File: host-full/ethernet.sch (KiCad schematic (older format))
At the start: 140 parts, among them J1 CONN_INTEGRALSTICK_MCU_HOST, J2 CONN_INTEGRALSTICK_FPGA_HOST, J3 0826-1G1T-23-F, J4 0826-1G1T-23-F, J5 0826-1G1T-23-F, J6 0826-1G1T-23-F, U1 KSZ9031RNX, U2 KSZ9031RNX, U3 ECS-1612MV-250-CN-TR, U4 ECS-1612MV-250-CN-TR, U5 KSZ9031RNX, U6 ECS-1612MV-250-CN-TR

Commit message: Finished initial schematic review
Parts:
- added C76, C79, C82: 4.7 uF, symbol device:C
- added C77, C78, C80, C81, C83, C84: 0.47 uF, symbol device:C
- added L10, L8, L9: 600R @ 100 MHz, symbol passive-azonenberg:INDUCTOR_PWROUT
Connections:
- net 1V2: now also L10.2, L8.2, L9.2
- net 1V8: no longer R24.1, R36.1
- net 3V3: now also R24.1, R36.1
- net ETH1_A1V2: now also C79.1, C80.1, C81.1, L9.1
- net ETH1_LED1_N_1V8: now also J2.43 (IO_1V8_CLK); no longer J2.67 (IO_1V8)
- net ETH1_LED2_N_1V8: now also J2.67 (IO_1V8); no longer J2.68 (IO_1V8)
- net ETH1_MDC: now also J2.56 (IO_1V8); no longer J2.53 (IO_1V8)
- net ETH1_MDIO: now also J2.59 (IO_1V8); no longer J2.50 (IO_1V8)
- net ETH1_RST_N: now also J2.53 (IO_1V8); no longer J2.56 (IO_1V8)
- net ETH1_RXD0: now also J2.65 (IO_1V8); no longer J2.44 (IO_1V8)
- net ETH1_RXD1: now also J2.62 (IO_1V8); no longer J2.47 (IO_1V8)
- net ETH1_RXD2: now also J2.61 (IO_1V8); no longer J2.48 (IO_1V8)
- net ETH1_RXD3: now also J2.60 (IO_1V8); no longer J2.49 (IO_1V8)
- net ETH1_RX_CLK: now also J2.41 (IO_1V8_CLK); no longer J2.43 (IO_1V8_CLK)
- net ETH1_RX_DV: now also J2.66 (IO_1V8); no longer J2.42 (IO_1V8)
- net ETH1_TXD0: now also J2.42 (IO_1V8); no longer J2.66 (IO_1V8)
- net ETH1_TXD1: now also J2.44 (IO_1V8); no longer J2.65 (IO_1V8)
- net ETH1_TXD2: now also J2.47 (IO_1V8); no longer J2.62 (IO_1V8)
- net ETH1_TXD3: now also J2.48 (IO_1V8); no longer J2.61 (IO_1V8)
- net ETH1_TX_CLK: now also J2.49 (IO_1V8); no longer J2.60 (IO_1V8)
- net ETH1_TX_EN: now also J2.50 (IO_1V8); no longer J2.59 (IO_1V8)
- net ETH2_A1V2: now also C76.1, C77.1, C78.1, L8.1
- net ETH3_A1V2: now also C82.1, C83.1, C84.1, L10.1
- net GND: now also C76.2, C77.2, C78.2, C79.2, C80.2, C81.2, C82.2, C83.2, C84.2
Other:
- moved on the sheet: C3, C39, C7

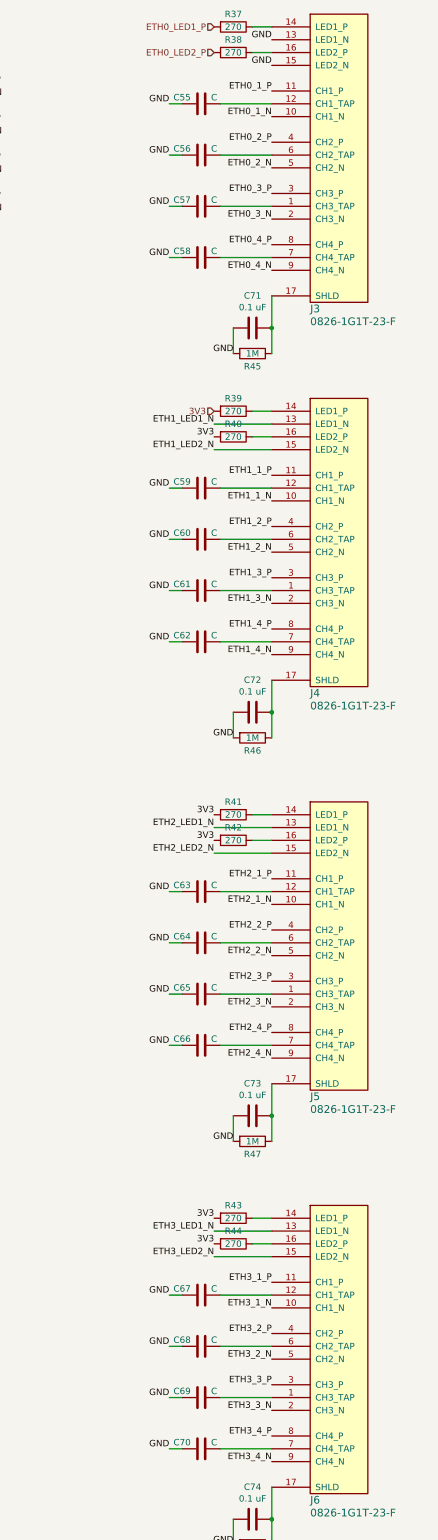
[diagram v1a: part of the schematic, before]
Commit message: Initial layout on host-full. Rough floorplan is finalized, all MCU PMODs routed.
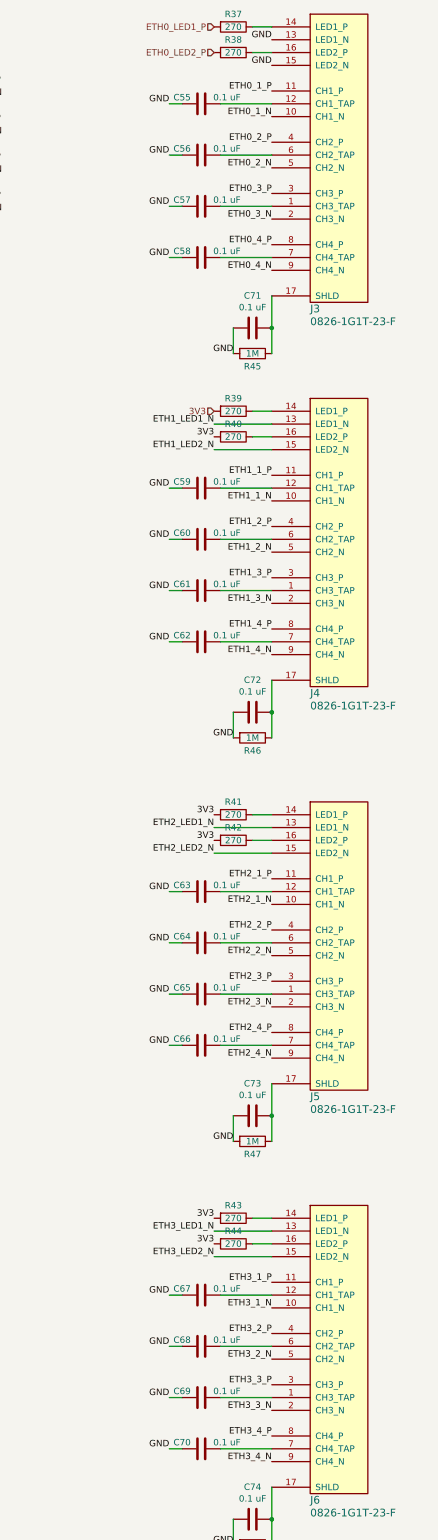
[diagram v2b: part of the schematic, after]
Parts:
- C1, C11, C13, C15, C2, C3, C37, C38, C39, C4, C40, C41, C43, C5, C6, C7, C76, C79, C8, C82, C9: footprint (none) -> azonenberg_pcb:EIA_0603_CAP_NOSILK
- C10, C12, C14, C16, C17, C18, C19, C20, C21, C22, C23, C24, C25, C26, C27, C28, C29, C30, C31, C32, C33, C34, C35, C36, C42, C44, C45, C46, C47, C48, C49, C50, C51, C52, C53, C54, C71, C72, C73, C74, C77, C78, C80, C81, C83, C84, L1, L10, L2, L3, L4, L5, L6, L8, L9: footprint (none) -> azonenberg_pcb:EIA_0402_CAP_NOSILK
- C55, C56, C57, C58, C59, C60, C61, C62, C63, C64, C65, C66, C67, C68, C69, C70: value C -> 0.1 uF; footprint (none) -> azonenberg_pcb:EIA_0402_CAP_NOSILK
- J1, J2: footprint (none) -> azonenberg_pcb:CONN_SAMTEC_QSH-060-01-L-D-A
- J3, J4, J5, J6: footprint (none) -> azonenberg_pcb:CONN_BELFUSE_0826_1G1T_23_F
- R1, R10, R11, R12, R13, R14, R15, R16, R17, R18, R19, R2, R20, R21, R22, R23, R24, R25, R26, R27, R28, R29, R3, R30, R31, R32, R33, R34, R35, R36, R37, R38, R39, R4, R40, R41, R42, R43, R44, R45, R46, R47, R48, R5, R6, R7, R8, R9: footprint (none) -> azonenberg_pcb:EIA_0402_RES_NOSILK
- U1, U2, U5: footprint (none) -> azonenberg_pcb:QFN_48_0.5MM_7x7MM
- U3, U4, U6: footprint (none) -> azonenberg_pcb:OSCILLATOR_1.6x1.2

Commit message: Continued host-full layout. Almost all PHY RGMII routing done
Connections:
- net 1V8: now also C38.1, C42.1, C46.1, C54.1, R36.1, U5.16 (DVDDH), U5.34 (DVDDH), U5.40 (DVDDH), U6.1 (E/D#), U6.4 (Vdd); no longer C10.1, C18.1, C2.1, C35.1, R17.1, R23.1, R8.1, U1.16 (DVDDH), U1.34 (DVDDH), U1.40 (DVDDH), U3.1 (E/D#), U3.4 (Vdd)
- net 3V3: now also C10.1, C18.1, C2.1, C35.1, R17.1, R23.1, R8.1, U1.16 (DVDDH), U1.34 (DVDDH), U1.40 (DVDDH), U3.1 (E/D#), U3.4 (Vdd); no longer C38.1, C42.1, C46.1, C54.1, R36.1, U5.16 (DVDDH), U5.34 (DVDDH), U5.40 (DVDDH), U6.1 (E/D#), U6.4 (Vdd)
- net ETH0_1_N: now also J1.4 (ETH_A_P); no longer J1.6 (ETH_A_N)
- net ETH0_1_P: now also J1.6 (ETH_A_N); no longer J1.4 (ETH_A_P)
- net ETH0_3_N: now also J1.16 (ETH_C_P); no longer J1.18 (ETH_C_N)
- net ETH0_3_P: now also J1.18 (ETH_C_N); no longer J1.16 (ETH_C_P)
- net ETH1_2_N: now also U1.5 (TXRXP_B); no longer U1.6 (TXRXM_B)
- net ETH1_2_P: now also U1.6 (TXRXM_B); no longer U1.5 (TXRXP_B)
- net ETH1_4_N: now also U1.10 (TXRXP_D); no longer U1.11 (TXRXM_D)
- net ETH1_4_P: now also U1.11 (TXRXM_D); no longer U1.10 (TXRXP_D)
- net ETH1_LED1_N: now also R19.2, U1.17 (LED1/PHYAD0); no longer J2.95 (IO_3V3)
- net ETH1_LED2_N: now also R1.2, U1.15 (LED2/PHYAD1); no longer J2.96 (IO_3V3)
- net ETH1_MDC: now also J2.79 (IO_3V3); no longer J2.56 (IO_1V8)
- net ETH1_MDIO: now also J2.77 (IO_3V3); no longer J2.59 (IO_1V8)
- net ETH1_RST_N: now also J2.73 (IO_3V3); no longer J2.53 (IO_1V8)
- net ETH1_RXD0: now also J2.85 (IO_3V3); no longer J2.65 (IO_1V8)
- net ETH1_RXD1: now also J2.89 (IO_3V3); no longer J2.62 (IO_1V8)
- net ETH1_RXD2: now also J2.91 (IO_3V3); no longer J2.61 (IO_1V8)
- net ETH1_RXD3: now also J2.95 (IO_3V3); no longer J2.60 (IO_1V8)
- net ETH1_RX_CLK: now also J2.71 (IO_3V3_CLK); no longer J2.41 (IO_1V8_CLK)
- net ETH1_RX_DV: now also J2.83 (IO_3V3); no longer J2.66 (IO_1V8)
- net ETH1_TXD0: now also J2.119 (IO_3V3); no longer J2.42 (IO_1V8)
- net ETH1_TXD1: now also J2.115 (IO_3V3); no longer J2.44 (IO_1V8)
- net ETH1_TXD2: now also J2.113 (IO_3V3); no longer J2.47 (IO_1V8)
- net ETH1_TXD3: now also J2.103 (IO_3V3); no longer J2.48 (IO_1V8)
- net ETH1_TX_CLK: now also J2.101 (IO_3V3); no longer J2.49 (IO_1V8)
- net ETH1_TX_EN: now also J2.97 (IO_3V3); no longer J2.50 (IO_1V8)
- net ETH2_2_N: now also U2.5 (TXRXP_B); no longer U2.6 (TXRXM_B)
- net ETH2_2_P: now also U2.6 (TXRXM_B); no longer U2.5 (TXRXP_B)
- net ETH2_4_N: now also U2.10 (TXRXP_D); no longer U2.11 (TXRXM_D)
- net ETH2_4_P: now also U2.11 (TXRXM_D); no longer U2.10 (TXRXP_D)
- net ETH2_MDC: now also J2.86 (IO_3V3); no longer J2.90 (IO_3V3)
- net ETH2_MDIO: now also J2.84 (IO_3V3); no longer J2.91 (IO_3V3)
- net ETH2_RST_N: now also J2.80 (IO_3V3); no longer J2.92 (IO_3V3)
- net ETH2_RXD0: now also J2.92 (IO_3V3); no longer J2.86 (IO_3V3)
- net ETH2_RXD1: now also J2.96 (IO_3V3); no longer J2.85 (IO_3V3)
- net ETH2_RXD2: now also J2.98 (IO_3V3); no longer J2.84 (IO_3V3)
- net ETH2_RXD3: now also J2.102 (IO_3V3); no longer J2.83 (IO_3V3)
- net ETH2_RX_CLK: now also J2.72 (IO_3V3_CLK); no longer J2.71 (IO_3V3_CLK)
- net ETH2_RX_DV: now also J2.90 (IO_3V3); no longer J2.89 (IO_3V3)
- net ETH2_TXD0: now also J2.120 (IO_3V3); no longer J2.73 (IO_3V3)
- net ETH2_TXD1: now also J2.116 (IO_3V3); no longer J2.74 (IO_3V3)
- net ETH2_TXD2: now also J2.114 (IO_3V3); no longer J2.77 (IO_3V3)
- net ETH2_TXD3: now also J2.110 (IO_3V3); no longer J2.78 (IO_3V3)
- net ETH2_TX_CLK: now also J2.108 (IO_3V3); no longer J2.79 (IO_3V3)
- net ETH2_TX_EN: now also J2.104 (IO_3V3); no longer J2.80 (IO_3V3)
- net ETH3_2_N: now also U5.5 (TXRXP_B); no longer U5.6 (TXRXM_B)
- net ETH3_2_P: now also U5.6 (TXRXM_B); no longer U5.5 (TXRXP_B)
- net ETH3_4_N: now also U5.10 (TXRXP_D); no longer U5.11 (TXRXM_D)
- net ETH3_4_P: now also U5.11 (TXRXM_D); no longer U5.10 (TXRXP_D)
- net ETH3_LED1_N: now also J2.78 (IO_3V3); no longer R34.2, U5.17 (LED1/PHYAD0)
- net ETH3_LED2_N: now also J2.74 (IO_3V3); no longer R25.2, U5.15 (LED2/PHYAD1)
- net ETH3_MDC: now also J2.43 (IO_1V8_CLK); no longer J2.116 (IO_3V3)
- net ETH3_MDIO: now also J2.42 (IO_1V8); no longer J2.119 (IO_3V3)
- net ETH3_RST_N: now also J2.44 (IO_1V8); no longer J2.120 (IO_3V3)
- net ETH3_RXD0: now also J2.49 (IO_1V8); no longer J2.114 (IO_3V3)
- net ETH3_RXD1: now also J2.53 (IO_1V8); no longer J2.113 (IO_3V3)
- net ETH3_RXD2: now also J2.55 (IO_1V8); no longer J2.110 (IO_3V3)
- net ETH3_RXD3: now also J2.59 (IO_1V8); no longer J2.108 (IO_3V3)
- net ETH3_RX_CLK: now also J2.41 (IO_1V8_CLK); no longer J2.72 (IO_3V3_CLK)
- net ETH3_RX_DV: now also J2.47 (IO_1V8); no longer J2.115 (IO_3V3)
- net ETH3_TXD0: now also J2.67 (IO_1V8); no longer J2.97 (IO_3V3)
- net ETH3_TXD1: now also J2.65 (IO_1V8); no longer J2.98 (IO_3V3)
- net ETH3_TXD2: now also J2.61 (IO_1V8); no longer J2.101 (IO_3V3)
- net ETH3_TXD3: now also J2.68 (IO_1V8); no longer J2.102 (IO_3V3)
- net ETH3_TX_CLK: now also J2.66 (IO_1V8); no longer J2.103 (IO_3V3)
- net ETH3_TX_EN: now also J2.62 (IO_1V8); no longer J2.104 (IO_3V3)
- net ETH3_LED1_N_1V8: now reaches J2.54 (IO_1V8)
- net ETH3_LED1_N_1V8: now also R34.2, U5.17 (LED1/PHYAD0)
- removed net ETH1_LED1_N_1V8: J2.43 (IO_1V8_CLK), R19.2, U1.17 (LED1/PHYAD0)
- removed net ETH1_LED2_N_1V8: J2.67 (IO_1V8), R1.2, U1.15 (LED2/PHYAD1)
- new net ETH3_LED2_N_1V8: J2.50 (IO_1V8), R25.2, U5.15 (LED2/PHYAD1)
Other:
- note added: "Pairs 1/3 swapped for routability"
- note added: "Pairs 2/4 swapped for routability"
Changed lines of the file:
@@
 Sheet 4 4
 Title "INTEGRALSTICK Full Host"
-Date "2019-11-07"
+Date "2019-11-08"
 Rev "0.1"
 Comp "Antikernel Labs"
@@
 Text Label 20100 3550 2    50   ~ 0
 GND
+Text Label 17950 1550 0    50   ~ 0
+ETH0_1_P
 Text Label 17950 1450 0    50   ~ 0
-ETH0_1_P
-Text Label 17950 1550 0    50   ~ 0
 ETH0_1_N
 Text Label 17950 1750 0    50   ~ 0
@@
 Text Label 17950 1850 0    50   ~ 0
 ETH0_2_N
+Text Label 17950 2150 0    50   ~ 0
+ETH0_3_P
 Text Label 17950 2050 0    50   ~ 0
-ETH0_3_P
-Text Label 17950 2150 0    50   ~ 0
 ETH0_3_N
-Text Label 17950 2350 0    50   ~ 0
-ETH0_4_P
 Text Label 17950 2450 0    50   ~ 0
 ETH0_4_N
@@
 Text Label 1450 3500 2    50   ~ 0
 ETH1_1_N
+Text Label 1450 3700 2    50   ~ 0
+ETH1_2_P
 Text Label 1450 3600 2    50   ~ 0
-ETH1_2_P
-Text Label 1450 3700 2    50   ~ 0
 ETH1_2_N
 Text Label 1450 3800 2    50   ~ 0
@@
 Text Label 1450 3900 2    50   ~ 0
 ETH1_3_N
+Text Label 1450 4100 2    50   ~ 0
+ETH1_4_P
 Text Label 1450 4000 2    50   ~ 0
-ETH1_4_P
-Text Label 1450 4100 2    50   ~ 0
 ETH1_4_N
 $Comp
@@
 	-1   0    0    1
 $EndComp
-Text HLabel 1450 1450 0    50   Input ~ 0
+Text HLabel 8250 8000 0    50   Input ~ 0
 1V8
 Text HLabel 1450 1950 0    50   Input ~ 0
@@
 3V3
 Text Label 4500 1350 0    50   ~ 0
-ETH1_LED1_N_1V8
+ETH1_LED1_N
 Wire Wire Line
 	4500 1350 4150 1350
 Connection ~ 4150 1350
 Text Label 4500 1250 0    50   ~ 0
-ETH1_LED2_N_1V8
+ETH1_LED2_N
 Wire Wire Line
 	4500 1250 3850 1250
@@
 Text Notes 4500 900  0    50   ~ 0
 Strap: PHYADR[1:0] = 2'b00
-Text Label 7200 2750 0    50   ~ 0
-ETH1_LED2_N_1V8
-Text Label 7200 1050 0    50   ~ 0
-ETH1_LED1_N_1V8
+Text Label 7200 1650 0    50   ~ 0
+ETH3_LED2_N_1V8
+Text Label 7200 1850 0    50   ~ 0
+ETH3_LED1_N_1V8
 Text HLabel 19950 4000 0    50   Input ~ 0
 3V3
@@
 Text Label 3700 2150 0    50   ~ 0
 ETH1_TX_EN
-Text Label 7200 1150 0    50   ~ 0
-ETH1_TXD0
-Text Label 7200 1250 0    50   ~ 0
-ETH1_TXD1
-Text Label 7200 1350 0    50   ~ 0
-ETH1_TXD2
-Text Label 7200 1450 0    50   ~ 0
-ETH1_TXD3
-Text Label 7200 1550 0    50   ~ 0
-ETH1_TX_CLK
-Text Label 7200 1650 0    50   ~ 0
-ETH1_TX_EN
+Text Label 7200 2750 0    50   ~ 0
+ETH3_TXD0
+Text Label 7200 2550 0    50   ~ 0
+ETH3_TXD1
+Text Label 7200 2350 0    50   ~ 0
+ETH3_TXD2
+Text Label 7200 2850 0    50   ~ 0
+ETH3_TXD3
+Text Label 7200 2650 0    50   ~ 0
+ETH3_TX_CLK
+Text Label 7200 2450 0    50   ~ 0
+ETH3_TX_EN
 Text Label 4100 2300 0    50   ~ 0
 ETH1_RXD3
@@
 $EndComp
 Text Label 5100 3000 0    50   ~ 0
-1V8
+3V3
 Wire Wire Line
 	5100 3000 4950 3000
@@
 $EndComp
 Text Label 4100 3200 0    50   ~ 0
-1V8
+3V3
 Wire Wire Line
 	4100 3200 4000 3200
@@
 Wire Wire Line
 	4100 3300 3700 3300
-Text Label 7200 2250 0    50   ~ 0
-ETH1_RXD3
-Text Label 7200 2350 0    50   ~ 0
-ETH1_RXD2
-Text Label 7200 2450 0    50   ~ 0
-ETH1_RXD1
-Text Label 7200 2550 0    50   ~ 0
-ETH1_RXD0
-Text Label 7200 2650 0    50   ~ 0
-ETH1_RX_DV
+Text Label 7200 2150 0    50   ~ 0
+ETH3_RXD3
+Text Label 7200 1950 0    50   ~ 0
+ETH3_RXD2
+Text Label 7200 1750 0    50   ~ 0
+ETH3_RXD1
+Text Label 7200 1550 0    50   ~ 0
+ETH3_RXD0
+Text Label 7200 1350 0    50   ~ 0
+ETH3_RX_DV
 Text Label 7200 950  0    50   ~ 0
-ETH1_RX_CLK
-Text Label 7200 2050 0    50   ~ 0
-ETH1_MDC
-Text Label 7200 2150 0    50   ~ 0
-ETH1_MDIO
-Text Label 7200 1750 0    50   ~ 0
-ETH1_RST_N
-NoConn ~ 7200 1950
-NoConn ~ 7200 1850
-NoConn ~ 7200 2850
+ETH3_RX_CLK
+Text Label 7200 1050 0    50   ~ 0
+ETH3_MDC
+Text Label 7200 1150 0    50   ~ 0
+ETH3_MDIO
+Text Label 7200 1250 0    50   ~ 0
+ETH3_RST_N
 $Comp
 L device:R R9
@@
 Connection ~ 6000 3650
 Text Label 6750 3650 0    50   ~ 0
-1V8
+3V3
 Wire Wire Line
 	6750 3650 6400 3650
@@
 ETH1_LED2_N
 Text Label 1250 5500 2    50   ~ 0
-1V8
+3V3
 $Comp
 L device:C C2
@@
 Text Label 1450 10050 2    50   ~ 0
 ETH2_1_N
+Text Label 1450 10250 2    50   ~ 0
+ETH2_2_P
 Text Label 1450 10150 2    50   ~ 0
-ETH2_2_P
-Text Label 1450 10250 2    50   ~ 0
 ETH2_2_N
 Text Label 1450 10350 2    50   ~ 0
@@
 Text Label 1450 10450 2    50   ~ 0
 ETH2_3_N
+Text Label 1450 10650 2    50   ~ 0
+ETH2_4_P
 Text Label 1450 10550 2    50   ~ 0
-ETH2_4_P
-Text Label 1450 10650 2    50   ~ 0
 ETH2_4_N
 $Comp
@@
 $EndComp
 Text Label 4100 9750 0    50   ~ 0
-1V8
+3V3
 Wire Wire Line
 	4100 9750 4000 9750
@@
 Text Label 8250 10050 2    50   ~ 0
 ETH3_1_N
+Text Label 8250 10250 2    50   ~ 0
+ETH3_2_P
 Text Label 8250 10150 2    50   ~ 0
-ETH3_2_P
-Text Label 8250 10250 2    50   ~ 0
 ETH3_2_N
 Text Label 8250 10350 2    50   ~ 0
 ETH3_3_P
-Text Label 8250 10450 2    50   ~ 0
-ETH3_3_N
-Text Label 8250 10550 2    50   ~ 0
+Text Label 8250 10650 2    50   ~ 0
 ETH3_4_P
-Text Label 8250 10650 2    50   ~ 0
-ETH3_4_N
 $Comp
 L device:R R25
@@
 $EndComp
 Text Label 11900 9550 0    50   ~ 0
-3V3
+1V8
 Wire Wire Line
 	11900 9550 11750 9550
@@
 Connection ~ 12800 10200
 Text Label 13550 10200 0    50   ~ 0
-3V3
+1V8
 Wire Wire Line
 	13550 10200 13200 10200
@@
 ETH3_TXD1
 Text Label 8050 12050 2    50   ~ 0
-3V3
+1V8
 $Comp
 L device:C C38
@@
 Wire Wire Line
 	10850 13400 11400 13400
-Text Label 8250 8000 2    50   ~ 0
+Text Label 1450 1450 2    50   ~ 0
 3V3
 Text Label 8250 8500 2    50   ~ 0
@@
 2V5
 Text Label 11300 7900 0    50   ~ 0
-ETH3_LED1_N
+ETH3_LED1_N_1V8
 Text Label 11300 7800 0    50   ~ 0
-ETH3_LED2_N
+ETH3_LED2_N_1V8
 Text Label 10500 8200 0    50   ~ 0
 ETH3_TXD0
@@
 	-1   0    0    -1
 $EndComp
+Text Label 9600 4250 0    50   ~ 0
+ETH2_TXD0
+Text Label 9600 3850 0    50   ~ 0
+ETH2_TXD2
+Text Label 9600 3650 0    50   ~ 0
+ETH2_TXD3
+Text Label 9600 3450 0    50   ~ 0
+ETH2_TX_CLK
+Text Label 9600 3250 0    50   ~ 0
+ETH2_TX_EN
+Text Label 9600 4050 0    50   ~ 0
+ETH2_TXD1
+Text Label 9600 3050 0    50   ~ 0
+ETH2_RXD3
+Text Label 9600 2850 0    50   ~ 0
+ETH2_RXD2
+Text Label 9600 2650 0    50   ~ 0
+ETH2_RXD1
+Text Label 9600 2450 0    50   ~ 0
+ETH2_RXD0
+Text Label 9600 2250 0    50   ~ 0
+ETH2_RX_DV
+Text Label 9600 1050 0    50   ~ 0
+ETH2_RX_CLK
+Text Label 9600 2050 0    50   ~ 0
+ETH2_MDC
+Text Label 9600 1850 0    50   ~ 0
+ETH2_MDIO
+Text Label 9600 1650 0    50   ~ 0
+ETH2_RST_N
+Text Label 9600 1450 0    50   ~ 0
+ETH3_LED1_N
+Text Label 9600 1250 0    50   ~ 0
+ETH3_LED2_N
+Text Label 9600 3750 0    50   ~ 0
+ETH1_TXD2
+Text Label 9600 3150 0    50   ~ 0
+ETH1_TXD3
+Text Label 9600 2950 0    50   ~ 0
+ETH1_TX_CLK
+Text Label 9600 2750 0    50   ~ 0
+ETH1_TX_EN
+Text Label 9600 3950 0    50   ~ 0
+ETH1_TXD1
+Text Label 9600 4150 0    50   ~ 0
+ETH1_TXD0
+Text Label 9600 2550 0    50   ~ 0
+ETH1_RXD3
+Text Label 9600 2350 0    50   ~ 0
+ETH1_RXD2
+Text Label 9600 2150 0    50   ~ 0
+ETH1_RXD1
+Text Label 9600 1950 0    50   ~ 0
+ETH1_RXD0
+Text Label 9600 1750 0    50   ~ 0
+ETH1_RX_DV
+Text Label 9600 950  0    50   ~ 0
+ETH1_RX_CLK
+Text Label 9600 1550 0    50   ~ 0
+ETH1_MDC
+Text Label 9600 1350 0    50   ~ 0
+ETH1_MDIO
 Text Label 9600 1150 0    50   ~ 0
-ETH2_TXD0
-Text Label 9600 1350 0    50   ~ 0
-ETH2_TXD2
-Text Label 9600 1450 0    50   ~ 0
-ETH2_TXD3
-Text Label 9600 1550 0    50   ~ 0
-ETH2_TX_CLK
-Text Label 9600 1650 0    50   ~ 0
-ETH2_TX_EN
-Text Label 9600 1250 0    50   ~ 0
-ETH2_TXD1
-Text Label 9600 1750 0    50   ~ 0
-ETH2_RXD3
-Text Label 9600 1850 0    50   ~ 0
-ETH2_RXD2
-Text Label 9600 1950 0    50   ~ 0
-ETH2_RXD1
-Text Label 9600 2050 0    50   ~ 0
-ETH2_RXD0
-Text Label 9600 2150 0    50   ~ 0
-ETH2_RX_DV
-Text Label 9600 950  0    50   ~ 0
-ETH2_RX_CLK
-Text Label 9600 2250 0    50   ~ 0
-ETH2_MDC
-Text Label 9600 2350 0    50   ~ 0
-ETH2_MDIO
-Text Label 9600 2450 0    50   ~ 0
-ETH2_RST_N
-Text Label 9600 2550 0    50   ~ 0
-ETH1_LED1_N
-Text Label 9600 2650 0    50   ~ 0
-ETH1_LED2_N
-Text Label 9600 2950 0    50   ~ 0
-ETH3_TXD2
-Text Label 9600 3050 0    50   ~ 0
-ETH3_TXD3
-Text Label 9600 3150 0    50   ~ 0
-ETH3_TX_CLK
-Text Label 9600 3250 0    50   ~ 0
-ETH3_TX_EN
-Text Label 9600 2850 0    50   ~ 0
-ETH3_TXD1
-Text Label 9600 2750 0    50   ~ 0
-ETH3_TXD0
-Text Label 9600 3450 0    50   ~ 0
-ETH3_RXD3
-Text Label 9600 3650 0    50   ~ 0
-ETH3_RXD2
-Text Label 9600 3750 0    50   ~ 0
-ETH3_RXD1
-Text Label 9600 3850 0    50   ~ 0
-ETH3_RXD0
-Text Label 9600 3950 0    50   ~ 0
-ETH3_RX_DV
-Text Label 9600 1050 0    50   ~ 0
-ETH3_RX_CLK
-Text Label 9600 4050 0    50   ~ 0
-ETH3_MDC
-Text Label 9600 4150 0    50   ~ 0
-ETH3_MDIO
-Text Label 9600 4250 0    50   ~ 0
-ETH3_RST_N
+ETH1_RST_N
 Text HLabel 10200 3350 2    50   Input ~ 0
 LVDS_CLK_N
@@
 	4950 5800 4400 5800
 Connection ~ 4400 5800
+Text Notes 1750 4300 0    50   ~ 0
+Pairs 2/4 swapped for routability
+Text Notes 1750 10850 0    50   ~ 0
+Pairs 2/4 swapped for routability
+Text Notes 8550 10850 0    50   ~ 0
+Pairs 2/4 swapped for routability
+Text Label 8250 10450 2    50   ~ 0
+ETH3_3_N
+Text Label 8250 10550 2    50   ~ 0
+ETH3_4_N
+Text Notes 17300 1350 0    50   ~ 0
+Pairs 1/3 swapped for routability
+Text Label 17950 2350 0    50   ~ 0
+ETH0_4_P
+NoConn ~ 7200 1450
+NoConn ~ 7200 2250
+NoConn ~ 7200 2050
 $EndSCHEMATC

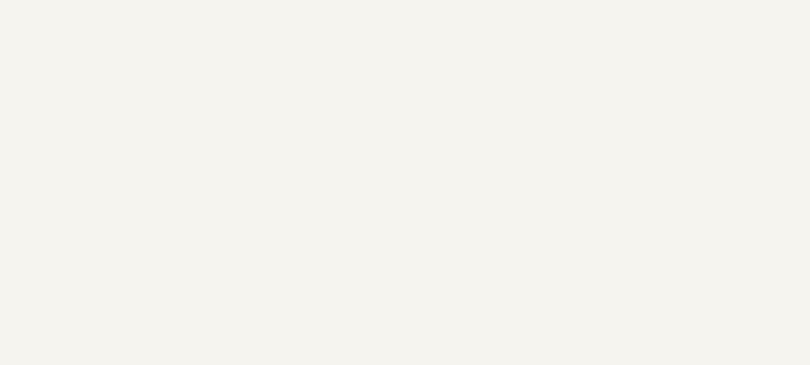
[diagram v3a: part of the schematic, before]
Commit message: Various fixes during layout review, added some silkscreen labels and a layer-change cap
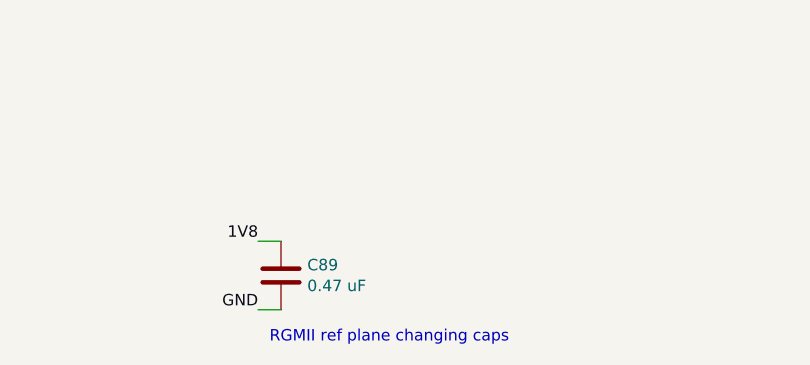
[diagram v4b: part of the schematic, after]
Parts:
- added C89: 0.47 uF, azonenberg_pcb:EIA_0402_CAP_NOSILK, symbol device:C
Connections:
- net 1V8: now also C89.1
- net GND: now also C89.2
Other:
- note added: "RGMII ref plane changing caps"
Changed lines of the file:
@@
 Sheet 4 4
 Title "INTEGRALSTICK Full Host"
-Date "2019-11-08"
+Date "2019-11-10"
 Rev "0.1"
 Comp "Antikernel Labs"
@@
 NoConn ~ 7200 2250
 NoConn ~ 7200 2050
+$Comp
+L device:C C89
+U 1 1 5EBB13E4
+P 14500 14950
+F 0 "C89" H 14615 14996 50  0000 L CNN
+F 1 "0.47 uF" H 14615 14905 50  0000 L CNN
+F 2 "azonenberg_pcb:EIA_0402_CAP_NOSILK" H 14538 14800 50  0001 C CNN
+F 3 "" H 14500 14950 50  0001 C CNN
+	1    14500 14950
+	1    0    0    -1
+$EndComp
+Text Notes 14450 15250 0    50   ~ 0
+RGMII ref plane changing caps
+Text Label 14400 14800 2    50   ~ 0
+1V8
+Wire Wire Line
+	14400 14800 14500 14800
+Text Label 14400 15100 2    50   ~ 0
+GND
+Wire Wire Line
+	14400 15100 14500 15100
 $EndSCHEMATC
